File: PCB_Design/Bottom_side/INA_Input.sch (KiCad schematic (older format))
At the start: 6 parts

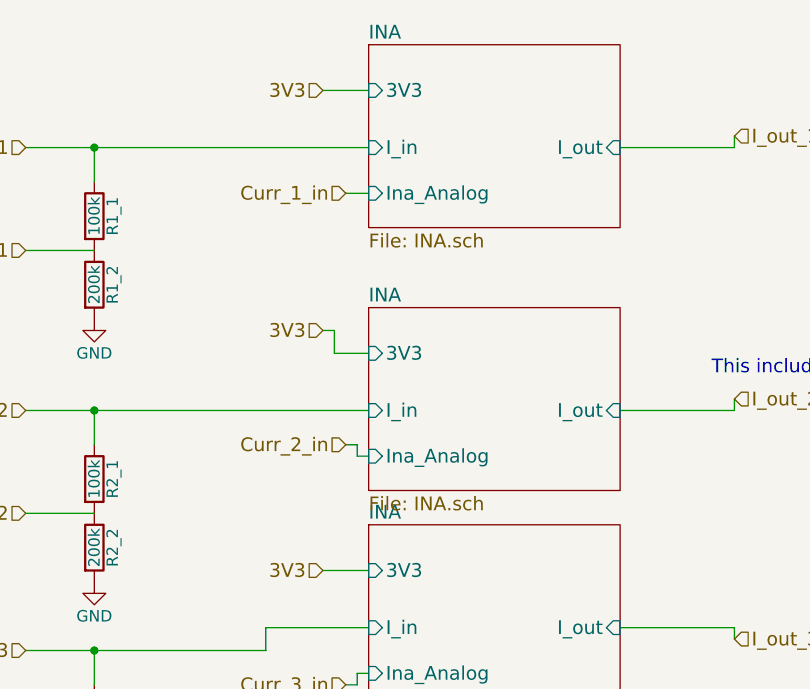
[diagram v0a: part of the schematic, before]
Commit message: PCB bottom layer populated
PCB bottom layer populated, and waiting for top layer to be merged.
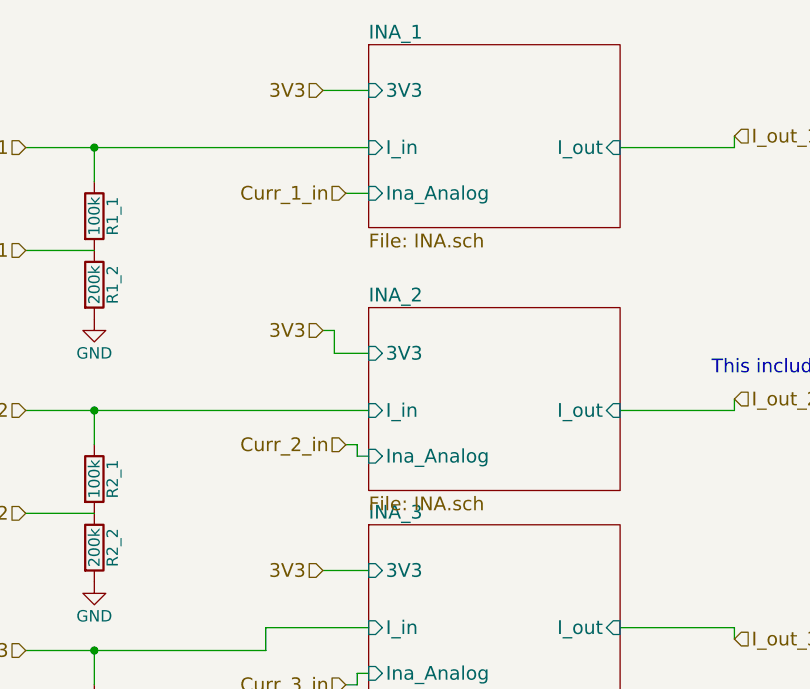
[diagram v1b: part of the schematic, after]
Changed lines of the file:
@@
 LIBS:contrib
 LIBS:valves
-LIBS:Custom_Library
 LIBS:Bottom_side-cache
 EELAYER 25 0
@@
 $Descr A4 11693 8268
 encoding utf-8
-Sheet 3 25
+Sheet 3 26
 Title ""
 Date ""
@@
 S 2550 1150 1100 800
 U 5A57B5E1
-F0 "INA" 60
+F0 "INA_1" 60
 F1 "INA.sch" 60
 F2 "3V3" I L 2550 1350 60
@@
 S 2550 2300 1100 800
 U 5A681ED4
-F0 "INA" 60
+F0 "INA_2" 60
 F1 "INA.sch" 60
 F2 "3V3" I L 2550 2500 60
@@
 S 2550 3250 1100 800
 U 5A6821BC
-F0 "INA" 60
+F0 "INA_3" 60
 F1 "INA.sch" 60
 F2 "3V3" I L 2550 3450 60

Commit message: Updated PCB structure tree
Full_PCB now includes bottom and top layer hierarchical sheets
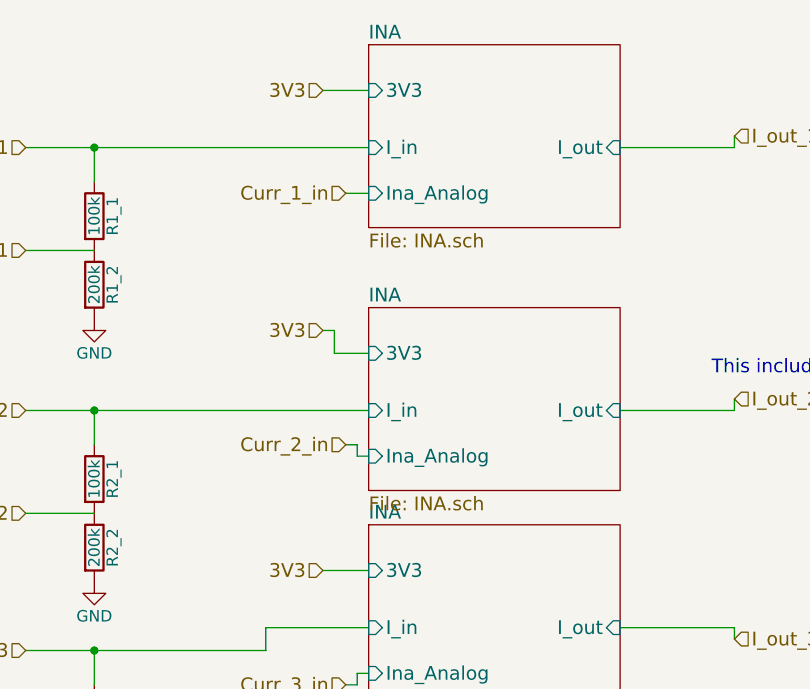
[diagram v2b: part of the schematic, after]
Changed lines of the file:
@@
 LIBS:power
 LIBS:device
-LIBS:switches
-LIBS:relays
-LIBS:motors
 LIBS:transistors
 LIBS:conn
@@
 LIBS:contrib
 LIBS:valves
-LIBS:Bottom_side-cache
+LIBS:Full_PCB-cache
 EELAYER 25 0
 EELAYER END
@@
 S 2550 1150 1100 800
 U 5A57B5E1
-F0 "INA_1" 60
+F0 "INA" 60
 F1 "INA.sch" 60
 F2 "3V3" I L 2550 1350 60
@@
 S 2550 2300 1100 800
 U 5A681ED4
-F0 "INA_2" 60
+F0 "INA" 60
 F1 "INA.sch" 60
 F2 "3V3" I L 2550 2500 60
@@
 S 2550 3250 1100 800
 U 5A6821BC
-F0 "INA_3" 60
+F0 "INA" 60
 F1 "INA.sch" 60
 F2 "3V3" I L 2550 3450 60
